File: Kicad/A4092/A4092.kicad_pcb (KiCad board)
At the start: 4 copper layers, 175.6 x 122.1 mm, 133 parts, among them CN1 Zorro3, J1 5749721-7, J2 5749721-7, J3 TO-LED, J4 TO-MB, J5 TO-A3000-LED, J6 TO-A3000-MB, J8 Conn_01x06_Pin, U1 SN74ABT16543DGGR, U10 DS21S07A, U11 DS21S07A, U12 DS21S07A, U13 W25X40CLSN, U2 SN74ABT16543DGGR, U3 SN74ABT16543DGGR, U4 SN74ABT16543DGGR, U5 74LVC07APW_118, U6 SN74ABT16543DGGR, U7 AMS1117-3.3, U8 XC95144XL-TQ144, U9 LSI53C770 SCSI Host Controller, Y1 Abracon ACO-50MHz, Y2 Abracon ACO-40MHz

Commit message: U9 data routing
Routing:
- net PLD_EXT_TERM: track 149.7 -> 0.00 mm, vias 1 -> 0
- net BCLK_FULL: track 0.00 -> 38.7 mm
- net D25: track 25.6 -> 55.4 mm, vias 0 -> 1
- net D24: track 25.3 -> 54.0 mm, vias 0 -> 1
- net D26: track 26.3 -> 54.1 mm, vias 0 -> 1
- net D28: track 28.0 -> 54.7 mm, vias 0 -> 1
- net D29: track 27.9 -> 53.6 mm, vias 0 -> 1
- net D27: track 26.8 -> 52.0 mm, vias 0 -> 1
- net D31: track 29.3 -> 54.5 mm, vias 0 -> 1
- net LEDR: track 0.00 -> 25.0 mm
- net D30: track 29.0 -> 53.7 mm, vias 0 -> 1
- net Z_A15D7: track 29.4 -> 50.8 mm
- net MASTER: track 143.3 -> 158.2 mm, vias 7 -> 8
- net LED3KPWR: track 0.00 -> 5.39 mm
- net Net-(D2-K): track 0.00 -> 2.73 mm
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
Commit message: General routing
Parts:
- removed R1: 4K7, Resistor_SMD:R_0603_1608Metric_Pad0.98x0.95mm_HandSolder
- removed R100, R101, R102, R103, R94, R95: 1K, Resistor_SMD:R_0603_1608Metric_Pad0.98x0.95mm_HandSolder
- moved C22 5.22 mm to (128.0, 135.0), turned to -90 degrees
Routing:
- net SCLK: track 1.85 -> 114.2 mm, vias 0 -> 2
- net PLD_READ: track 21.4 -> 130.8 mm, vias 1 -> 4
- net A21: track 71.0 -> 118.8 mm, vias 3 -> 4
- net A22: track 71.7 -> 116.2 mm, vias 3 -> 4
- net PLD_SIZ0: track 5.87 -> 37.4 mm
- net Z_INT2: track 128.3 -> 159.6 mm, vias 2 -> 3
- net D0: track 22.3 -> 40.5 mm
- net A17: track 119.2 -> 132.4 mm, vias 4 -> 5
- net MASTER: track 158.2 -> 170.1 mm
- net GND: track 139.8 -> 128.3 mm, vias 293 -> 284
- net D24: track 54.0 -> 63.9 mm, vias 1 -> 2
- net D25: track 55.4 -> 65.3 mm, vias 1 -> 2
- net D27: track 52.0 -> 61.5 mm, vias 1 -> 2
- net DBLT: track 115.1 -> 124.3 mm, vias 4 -> 5
- net Z2D: track 97.8 -> 107.0 mm
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
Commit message: General routing
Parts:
- moved C21 9.06 mm to (120.0, 135.5), turned to -90 degrees
- moved C31 6.18 mm to (143.0, 120.5), turned to 90 degrees
- moved C33 5.59 mm to (143.0, 135.5), turned to -90 degrees
- moved C41 3.04 mm to (173.0, 120.5), turned to 90 degrees
- moved C43 2.06 mm to (173.0, 135.5), turned to -90 degrees
- moved C42 1.58 mm to (165.5, 135.5), turned to -90 degrees
- moved C30 1.12 mm to (150.5, 120.5), turned to 90 degrees
- moved C32 1.12 mm to (150.5, 135.5), turned to -90 degrees
- moved C22 0.50 mm to (128.0, 135.5)
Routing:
- net V5: track 188.2 -> 227.9 mm, vias 21 -> 19
- net NCR_INT: track 0.00 -> 22.4 mm, vias 0 -> 1
- net D15: track 14.8 -> 35.5 mm, vias 0 -> 1
- net Z_A25D25: track 54.7 -> 70.5 mm, vias 4 -> 3
- net A18: track 83.7 -> 96.5 mm, vias 4 -> 5
- net A19: track 109.7 -> 99.0 mm, vias 4 -> 5
- net DBOE: track 127.8 -> 136.0 mm, vias 3 -> 4
- net GND: track 128.3 -> 120.6 mm, vias 284 -> 275
- net PLD_FC1: track 151.8 -> 145.9 mm
- net A31: track 98.8 -> 103.8 mm, vias 3 -> 4
- net A30: track 102.4 -> 107.4 mm, vias 3 -> 4
- net A29: track 99.2 -> 104.2 mm, vias 3 -> 4
- net PLD_SIZ1: track 34.3 -> 30.8 mm
- net IORST: track 73.0 -> 75.7 mm
- net Z2D: track 107.0 -> 109.5 mm, vias 5 -> 7
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
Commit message: Routing
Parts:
- moved C10 1.80 mm to (87.0, 120.5), turned to 90 degrees
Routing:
- net PLD_DS: track 2.86 -> 72.7 mm, vias 0 -> 1
- net IORST: track 75.7 -> 141.4 mm, vias 2 -> 3
- net BCLK_FULL: track 38.7 -> 64.5 mm, vias 0 -> 2
- net SCLK: track 113.3 -> 138.0 mm, vias 2 -> 4
- net PLD_SIZ1: track 30.8 -> 51.2 mm, vias 1 -> 2
- net D15: track 35.5 -> 51.7 mm
- net PLD_SIZ0: track 37.4 -> 51.1 mm
- net D0: track 40.5 -> 49.6 mm, vias 0 -> 2
- net MASTER: track 170.0 -> 176.7 mm
- net PLD_AS: track 35.8 -> 41.2 mm
- net SLACK: track 76.8 -> 80.6 mm
- net GND: track 120.6 -> 117.5 mm, vias 275 -> 273
- net V5: track 227.9 -> 224.8 mm
- net D2Z: track 89.0 -> 91.6 mm, vias 2 -> 3
- net A0: track 48.2 -> 45.9 mm
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
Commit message: Routing
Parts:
- moved R107 10.2 mm to (133.5, 114.0)
- moved C20 3.64 mm to (135.0, 122.5), turned to 90 degrees
- moved C95 3.00 mm to (148.5, 114.5)
- moved C6 2.72 mm to (183.5, 109.0), turned to 180 degrees
- moved D1 2.00 mm to (183.5, 103.3)
- moved F1 1.75 mm to (183.5, 97.5)
- moved C90 0.50 mm to (120.0, 87.0)
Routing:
- net SCSI_BUSY: track 95.9 -> 262.1 mm, vias 3 -> 8
- net PLD_EXT_TERM: track 0.00 -> 152.0 mm, vias 0 -> 2
- net PLD_MTCR: track 29.3 -> 141.1 mm, vias 1 -> 4
- net SREG: track 0.00 -> 68.0 mm, vias 0 -> 1
- net SC0: track 0.00 -> 57.0 mm, vias 0 -> 2
- net NCR_INT: track 22.4 -> 67.0 mm
- net SCDAT12: track 67.9 -> 110.4 mm, vias 1 -> 2
- net SCSI_TERMPWR: track 47.4 -> 89.6 mm, vias 0 -> 1
- net TDO: track 16.3 -> 55.7 mm, vias 0 -> 3
- net SCDAT13: track 99.0 -> 137.5 mm, vias 2 -> 5
- net SCDAT15: track 97.7 -> 133.8 mm, vias 2 -> 5
- net SCDAT14: track 95.1 -> 129.9 mm, vias 2 -> 5
- net SCDATP1: track 93.9 -> 127.8 mm, vias 2 -> 5
- net SCTRL_RST: track 91.0 -> 124.3 mm, vias 3 -> 4
- net SCTRL_CD: track 100.0 -> 132.9 mm, vias 3 -> 5
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
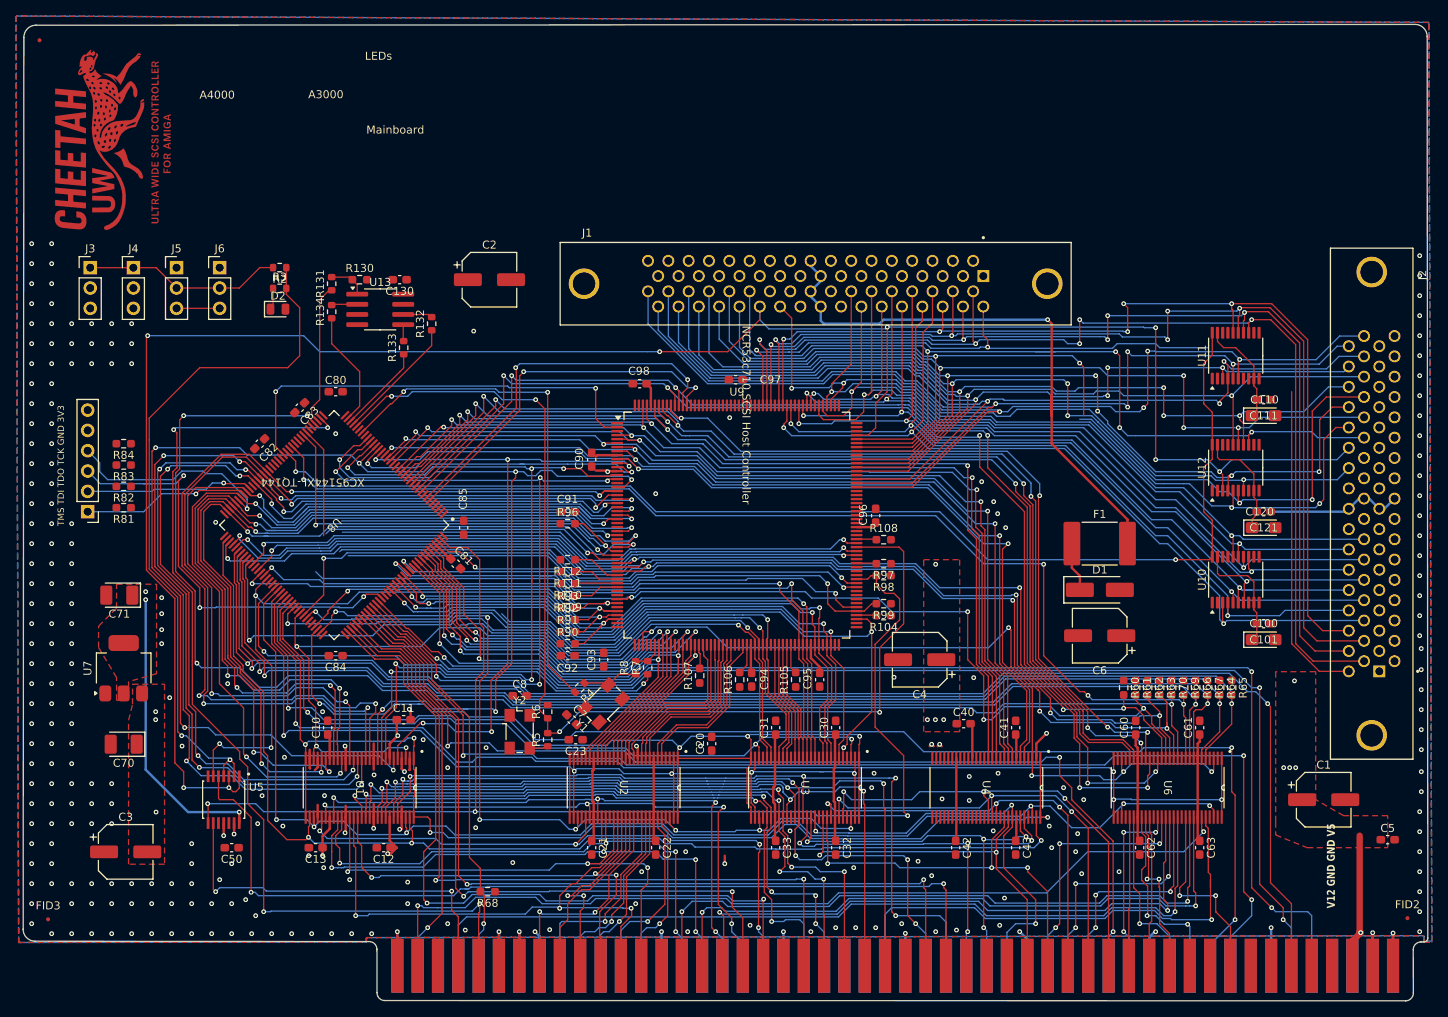
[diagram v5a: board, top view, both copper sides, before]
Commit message: Fix up graphics in PCB
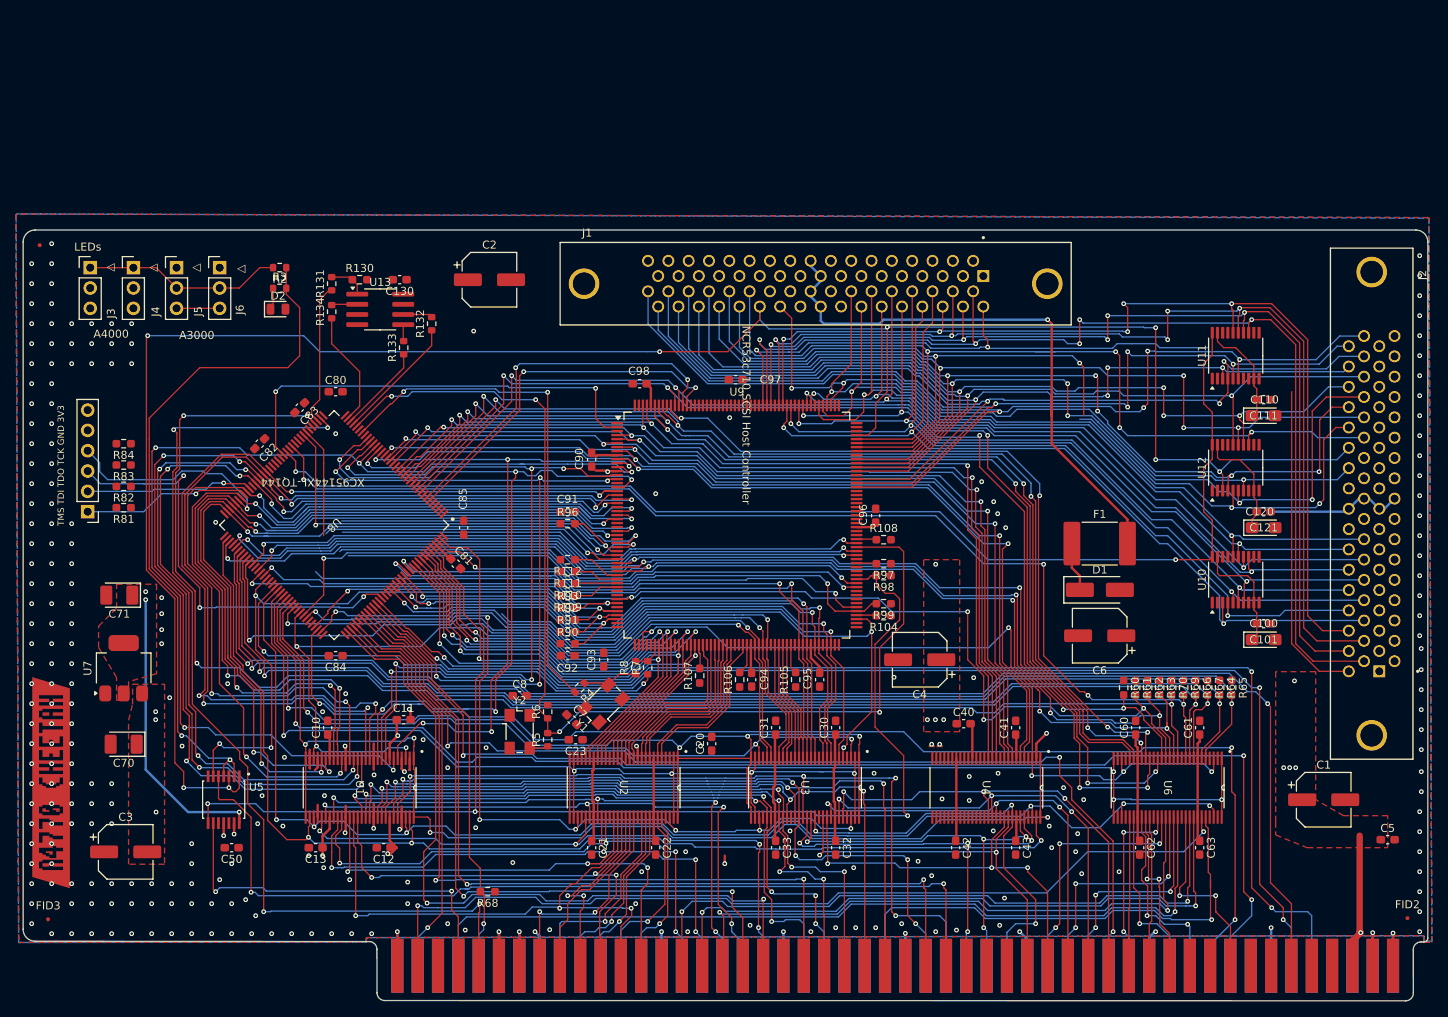
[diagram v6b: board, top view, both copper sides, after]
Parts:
- added kibuzzard-696E6D75: G***, kibuzzard-696E6D75, F.Cu at (52.4, 127.4)
- moved FID1 25.6 mm to (51.0, 60.2)
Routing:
- net GND: vias 274 -> 273
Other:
- board size 175.6 x 122.1 mm -> 175.6 x 96.4 mm
- board text added: "PCB Design: Monse Almaraz Schematics: Stefan Reinauer Special thanks to: Chris Hooper, Salih Albayrak, Dorken, Eduardo Michel, Matt Harlum A4091 by: DH/SS/GB/FISH"
- board text added: "REV A 2026/01/19"
- board text added: "◁"
- board text removed: "Can we get to this height?"
- board text removed: "Mainboard"
- board text removed: "PCB: Monse Almaraz Schematics: Stefan Reinauer Special thanks to: Chris Hooper, Salih Albayrak, Eduardo Michel Matt Harlum, Dorken Original A4091: DH/SS/GB/FISH"
- board text removed: "REV A 2025/06/01"
- board text removed: "V12 GND GND V5"
